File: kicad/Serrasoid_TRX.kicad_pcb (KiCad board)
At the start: 4 copper layers, 170 x 130 mm, 247 parts, among them J1 DC 13.8V, J2 I2C, J3 TJC, J4 ENC, J5 ANT, J6 TX LED, J7 MIC, J8 VOL, J9 SP, K1 G5V-2 DC12, Q1 2SC1815, Q2 2SA1015, Q3 2N7000, Q4 2N3866, Q5 RD06HHF1, Q6 RD16HHF1, Q7 2N3819, Q8 2SC1815, T1 BN43-202 2T:5T, U1 R-78E5.0-1.0, U10 74AC14, U11 74AC86, U12 74AC86, U13 MCP6004, U14 SA612AN, U15 MC3361, U16 LM386N-1, U17 78L05, U18 MCP6002, U2 L7808, U3 L7805, U4 LP2950-3.3, U5 XIAO ESP32C3, U6 AE-Si5351A, U7 74HCT4017, U8 MAX913CPA, U9 74HCT123, X1 10.245MHz, X2 CDBM455C24

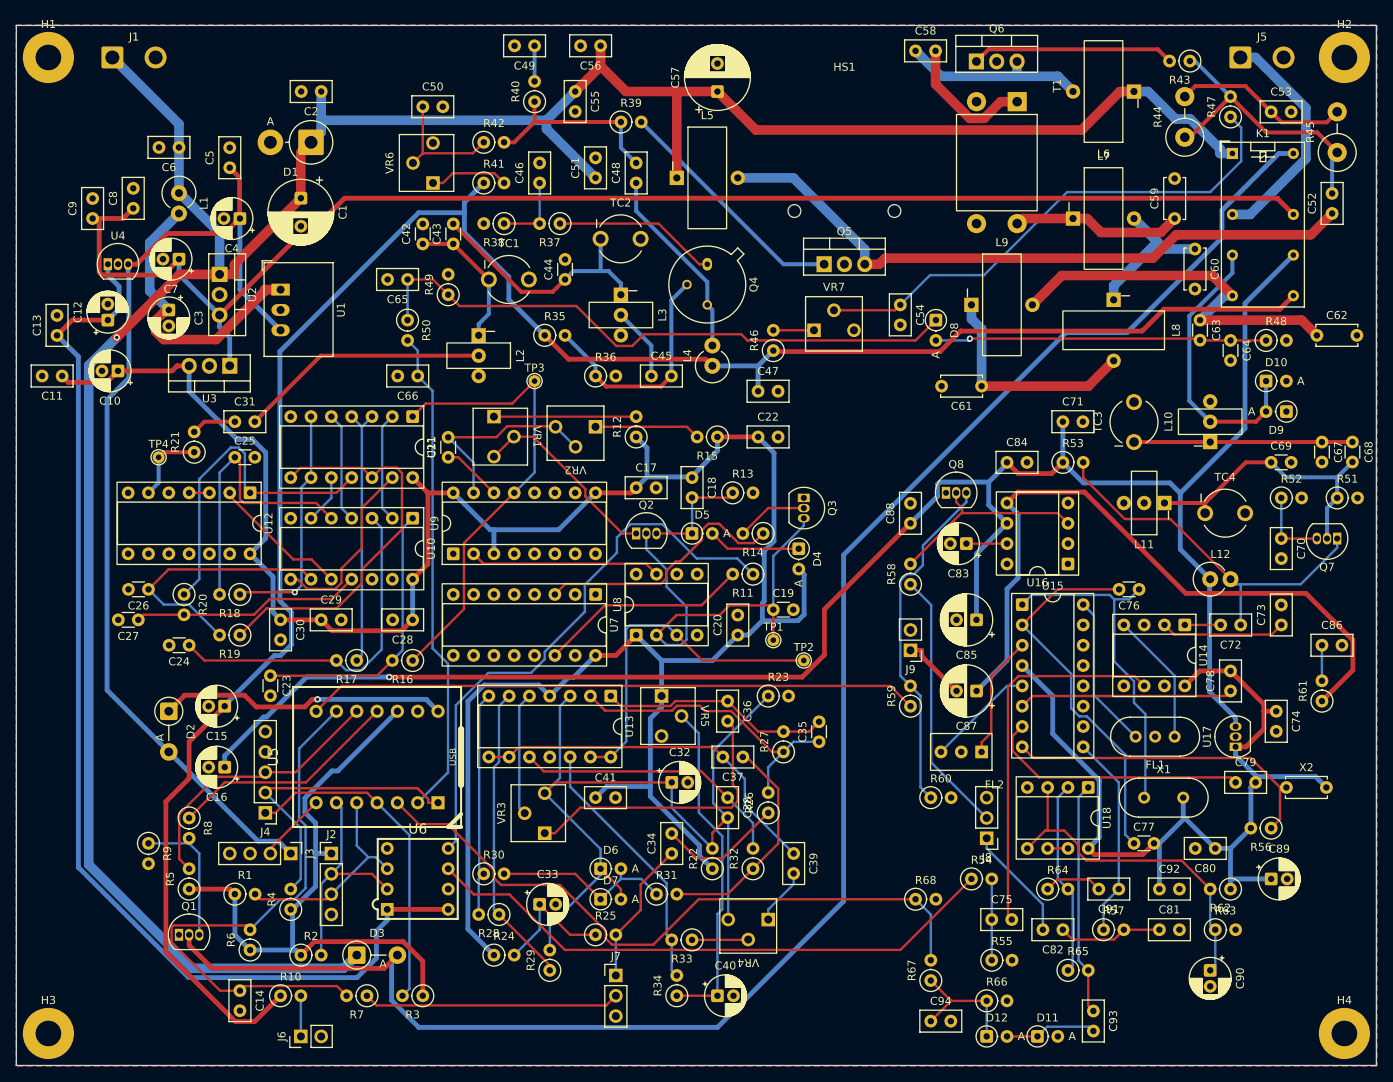
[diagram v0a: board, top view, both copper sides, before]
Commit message: 回路図の論理チェック（第 2 回）: 2 件修正し、基板を作り直す
- XIAO の D0（GPIO2、起動時に High が必要）からエンコーダ B 相を外し、D0 = PTT、D8 = エンコーダ B 相に
- SA612 の局発入力を範囲（200〜300mVp-p）の中央に: R54 1k → 1.2kΩ（約 0.25Vp-p）
- C58 は積層セラミック（約 1.6Arms）と部品表に明記
- PTT・エンコーダ周りの回路図の配置を、ピンの入れ替えに合わせて手で置き直す
- 回路図: ERC 違反なし、接続照合 655 ピン一致。基板: 配置・配線をやり直し DRC エラー 0・未接続 0・食い違い 0
- 結果を docs/回路図論理チェック.md に追記、README の XIAO のピン表を更新

Co-Authored-By: Claude Opus 5.5 <noreply@anthropic.com>
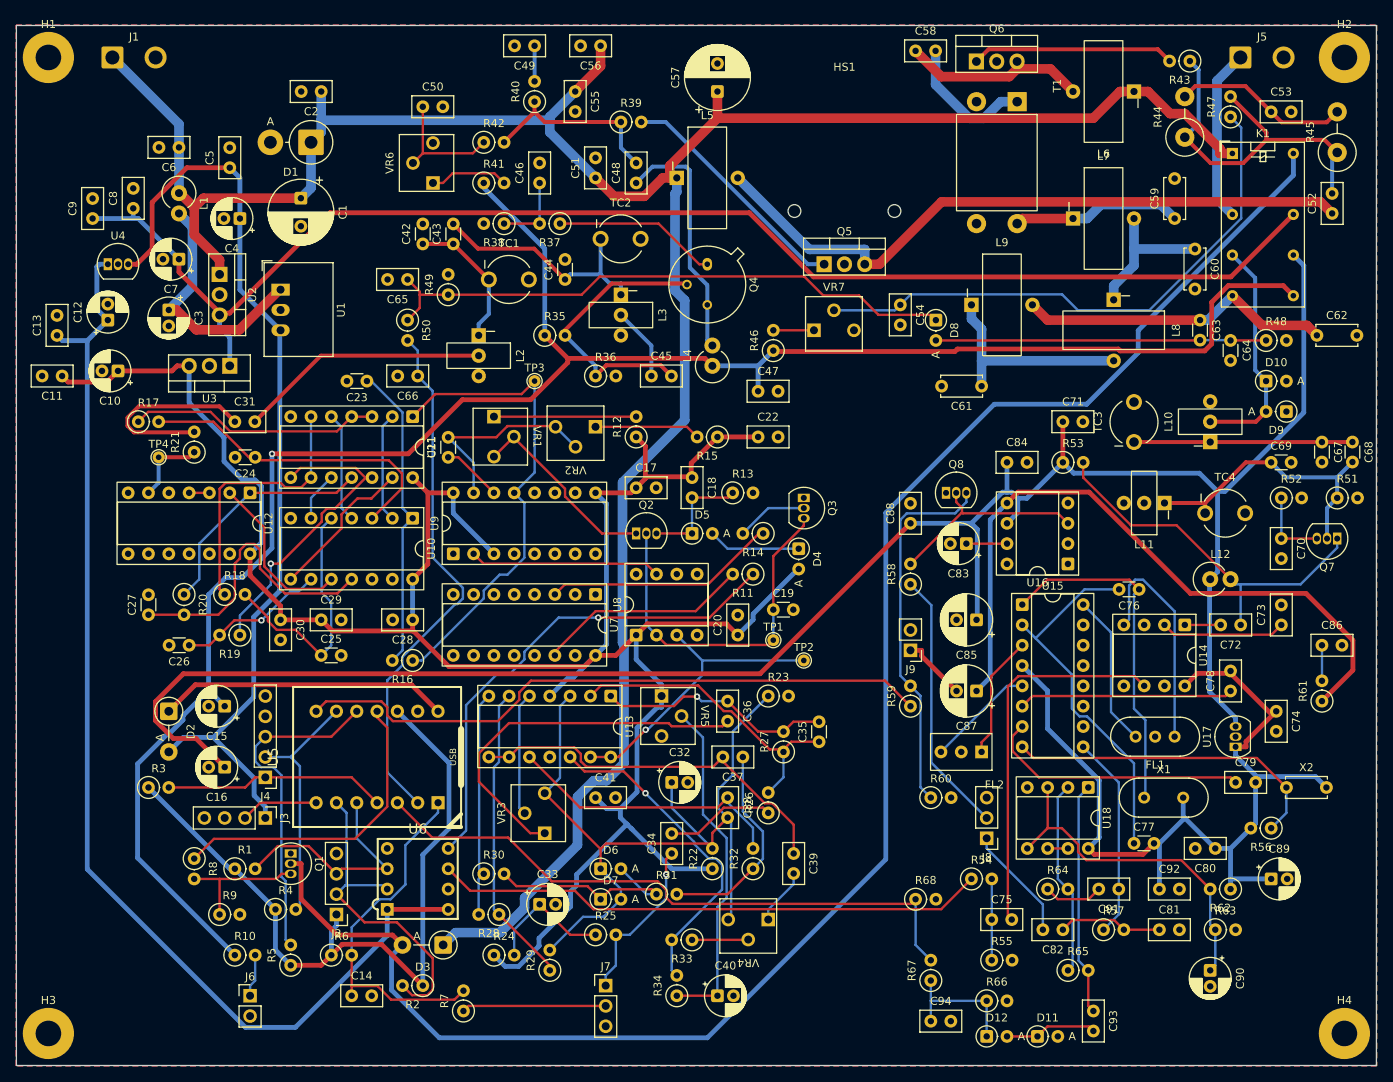
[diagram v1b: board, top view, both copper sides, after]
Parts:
- R54: value 1k -> 1.2k
- moved R3 43.1 mm to (16.5, 95.2), turned to 0 degrees
- moved R17 40.5 mm to (15.2, 49.5), turned to 0 degrees
- moved C23 38.8 mm to (43.8, 44.5), turned to 180 degrees
- moved C25 27.0 mm to (38.1, 78.7)
- moved C24 24.9 mm to (29.8, 54.0)
- moved Q1 17.3 mm to (34.3, 103.5), turned to -90 degrees
- moved R5 15.9 mm to (34.3, 117.5)
- moved R2 15.7 mm to (50.8, 120.0), turned to 180 degrees
- moved C14 14.0 mm to (41.9, 121.3), turned to 0 degrees
- moved R9 12.6 mm to (25.4, 111.1), turned to 0 degrees
- moved R7 12.2 mm to (55.9, 123.2), turned to 90 degrees
- moved D3 10.9 mm to (53.3, 114.9), turned to 180 degrees
- moved R6 10.2 mm to (39.4, 116.2), turned to 0 degrees
- moved C26 8.64 mm to (21.6, 77.5)
- moved J6 8.13 mm to (29.2, 121.3), turned to 0 degrees
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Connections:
- C14 pad 1: Net-(U5-D8/SCK) -> Net-(U5-D0/A0)
- R6 pad 2: Net-(U5-D8/SCK) -> Net-(U5-D0/A0)
- R7 pad 2: Net-(U5-D8/SCK) -> Net-(U5-D0/A0)
- U5 pad 1: Net-(J4-Pin_2) -> Net-(U5-D0/A0)
- U5 pad 13: Net-(U5-D8/SCK) -> Net-(J4-Pin_2)
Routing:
- net Net-(U5-D8/SCK): track 70.6 -> 0.00 mm
- net Net-(U5-D0/A0): track 0.00 -> 44.5 mm
- net Net-(C31-Pad1): track 5.61 -> 24.5 mm
- net RX8V: track 235.7 -> 251.9 mm, vias 1 -> 0
- net +13V8: track 333.6 -> 319.0 mm, vias 1 -> 0
- net Net-(C26-Pad1): track 33.1 -> 18.7 mm, vias 0 -> 1
- net Net-(J7-Pin_2): track 32.1 -> 18.0 mm
- net Net-(J4-Pin_1): track 41.7 -> 27.9 mm
- net Net-(J2-Pin_2): track 28.1 -> 41.7 mm
- net +3V3X: track 80.6 -> 93.4 mm
- net Net-(R20-Pad1): track 41.5 -> 29.6 mm
- net Net-(FL1-IN): track 16.6 -> 28.5 mm
- net Net-(C36-Pad2): track 36.3 -> 47.5 mm
- net Net-(R19-Pad1): track 49.5 -> 38.6 mm, vias 0 -> 1
- net Net-(U5-D10/MOSI): track 29.0 -> 39.3 mm
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
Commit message: 部品番号を回路図の位置順に振り直す（PSN_TRX 2026-10-15 と同じ方法）
- 種類ごとに回路図の X の小さい順、同じ X は Y の順（多ユニットは最も小さいユニットの位置）。242 点のうち 206 点が変更
- tools/renumber.py: 回路図・基板の部品番号と、番号から作る UUID、基板のネット名（Net-(C23-Pad1) など 140 個）を書き換え、
  circuit.py の RENUMBER（仮の番号 → 最終の番号）・LAYOUT・注記、資料・ケースの番号も置き換える
- 新旧の対応表 kicad/refdes_map_2026-10-16.csv。チェックの記録（回路図論理チェック・基板チェック）は旧番号のまま注記
- 確認: 回路図と circuit.py の照合 655 ピン一致、ERC 0、DRC エラー 0・未接続 0・回路図との食い違い 0（シルクの警告のみ）、
  LAYOUT と回路図の位置がブロックごとに一致
- 部品表・回路図 PDF・部品実装図・A3 配置図・動作説明 docx を作り直し

Co-Authored-By: Claude Opus 5.5 <noreply@anthropic.com>
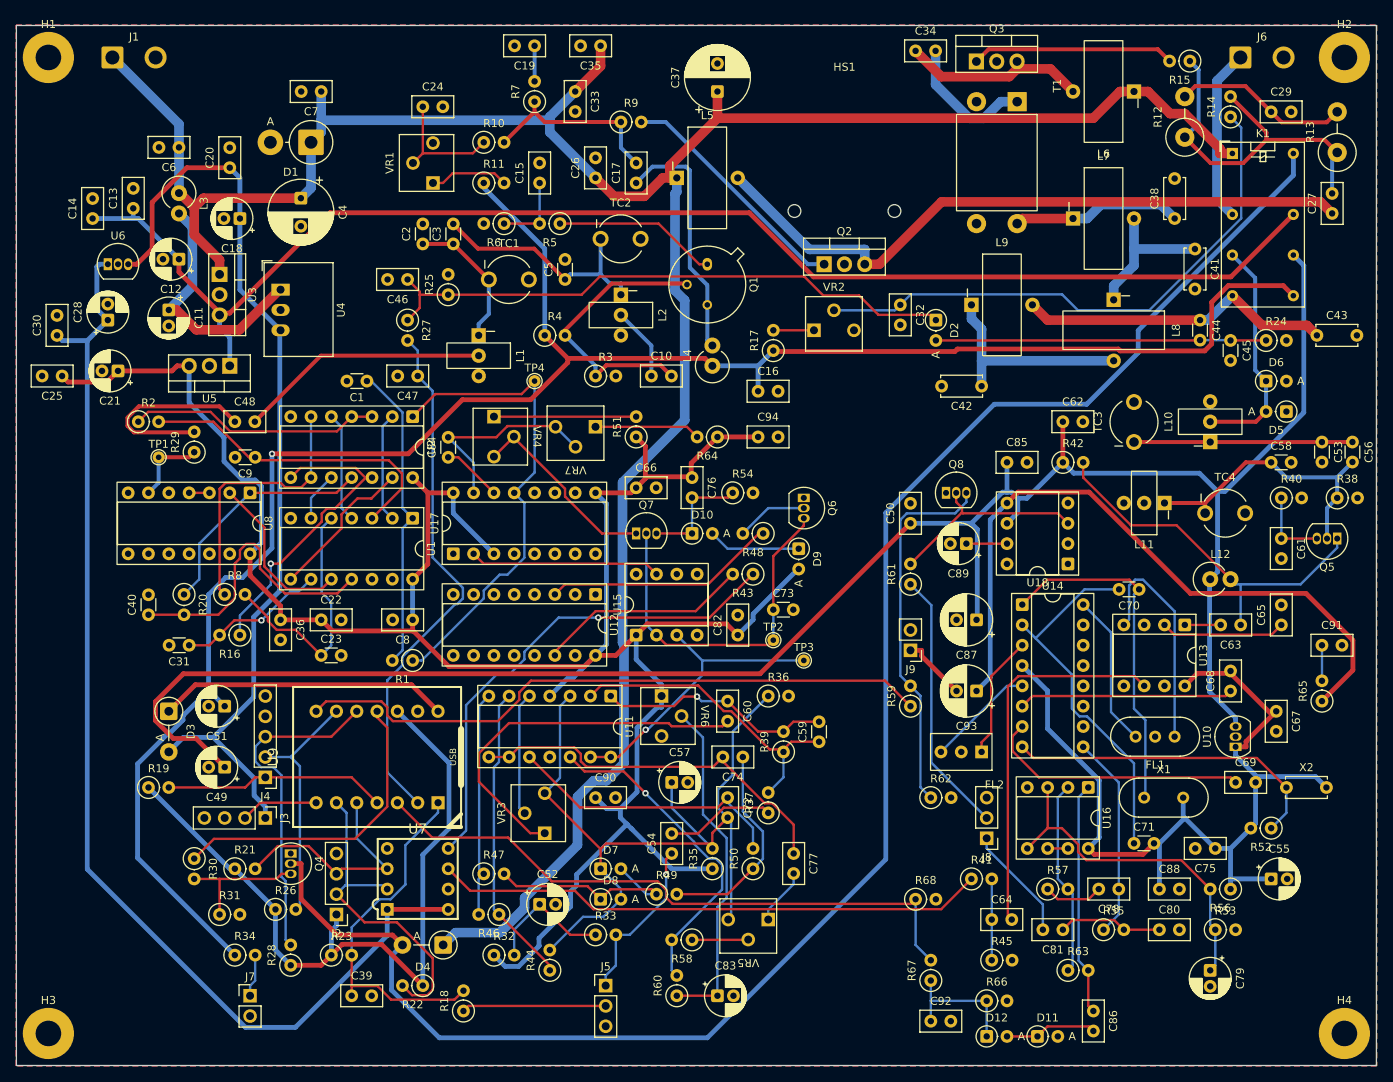
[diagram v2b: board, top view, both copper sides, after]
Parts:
- renumbered C23 to C1, C45 to C10, C3 to C11, C7 to C12, C8 to C13, C9 to C14, C46 to C15, C47 to C16, C48 to C17, C4 to C18, C49 to C19, C42 to C2, C5 to C20, C10 to C21, C29 to C22, C25 to C23, C50 to C24, C11 to C25, C51 to C26, C52 to C27, C12 to C28, C53 to C29, C43 to C3, C13 to C30, C26 to C31, C54 to C32, C55 to C33, C58 to C34, C56 to C35, C30 to C36, C57 to C37, C59 to C38, C14 to C39, C1 to C4, C27 to C40, C60 to C41, C61 to C42, C62 to C43, C63 to C44, C64 to C45, C65 to C46, C66 to C47, C31 to C48, C16 to C49, C44 to C5, C88 to C50, C15 to C51, C33 to C52, C67 to C53, C34 to C54, C89 to C55, C68 to C56, C32 to C57, C69 to C58, C35 to C59, C36 to C60, C70 to C61, C71 to C62, C72 to C63, C75 to C64, C73 to C65, C17 to C66, C74 to C67, C78 to C68, C79 to C69, C2 to C7, C76 to C70, C77 to C71, C38 to C72, C19 to C73, C37 to C74, C80 to C75, C18 to C76, C39 to C77, C91 to C78, C90 to C79, C28 to C8, C81 to C80, C82 to C81, C20 to C82, C40 to C83, C21 to C84, C84 to C85, C93 to C86, C85 to C87, C92 to C88, C83 to C89, C24 to C9, C41 to C90, C86 to C91, C94 to C92, C87 to C93, C22 to C94, D5 to D10, D8 to D2, D2 to D3, D3 to D4, D9 to D5, D10 to D6, D6 to D7, D7 to D8, D4 to D9, J7 to J5, J5 to J6, J6 to J7, L2 to L1, L3 to L2, L1 to L3, Q4 to Q1, Q5 to Q2, Q6 to Q3, Q1 to Q4, Q7 to Q5, Q3 to Q6, Q2 to Q7, R16 to R1, R42 to R10, R41 to R11, R44 to R12, R45 to R13, R47 to R14, R43 to R15, R19 to R16, R46 to R17, R7 to R18, R3 to R19, R17 to R2, R1 to R21, R2 to R22, R6 to R23, R48 to R24, R49 to R25, R4 to R26, R50 to R27, R5 to R28, R21 to R29, R36 to R3, R8 to R30, R9 to R31, R24 to R32, R25 to R33, R10 to R34, R22 to R35, R23 to R36, R26 to R37, R51 to R38, R27 to R39, R35 to R4, R52 to R40, R54 to R41, R53 to R42, R11 to R43, R29 to R44, R55 to R45, R28 to R46, R30 to R47, R14 to R48, R31 to R49, R37 to R5, R32 to R50, R12 to R51, R56 to R52, R63 to R53, R13 to R54, R57 to R55, R62 to R56, R64 to R57, R33 to R58, R38 to R6, R34 to R60, R58 to R61, R60 to R62, R65 to R63, R15 to R64, R61 to R65, R40 to R7, R18 to R8, R39 to R9, TP4 to TP1, TP1 to TP2, TP2 to TP3, TP3 to TP4, U10 to U1, U17 to U10, U13 to U11, U7 to U12, U14 to U13, U15 to U14, U8 to U15, U18 to U16, U9 to U17, U16 to U18, U11 to U2, U2 to U3, U1 to U4, U3 to U5, U4 to U6, U6 to U7, U12 to U8, U5 to U9, VR6 to VR1, VR7 to VR2, VR1 to VR4, VR4 to VR5, VR5 to VR6, VR2 to VR7
